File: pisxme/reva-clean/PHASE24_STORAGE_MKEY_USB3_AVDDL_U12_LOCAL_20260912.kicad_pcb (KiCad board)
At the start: 6 copper layers, 300 x 180 mm, 131 parts, among them J1 74221-101LF, J2 A70-112-331N126, J3 1-2199230-4, J4 Amphenol 10171746-00021LF USB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, J5 0039300020, J6 0039300020, J7 Raspberry-Pi-5-Compute-Module, Q1 CSD19536KCS, Q2 CSD19536KCS, U1 LM74700QDBVRQ1, U2 LM74700QDBVRQ1, U3 TPSM63606RDLR, U4 TPSM63606RDLR, U5 TPSM63606RDLR, U6 TPD4EUSB30, U7 TUSB9261IPVP, U8 Texas_DRT_3, U9 TPD4EUSB30, Y10 25MHz

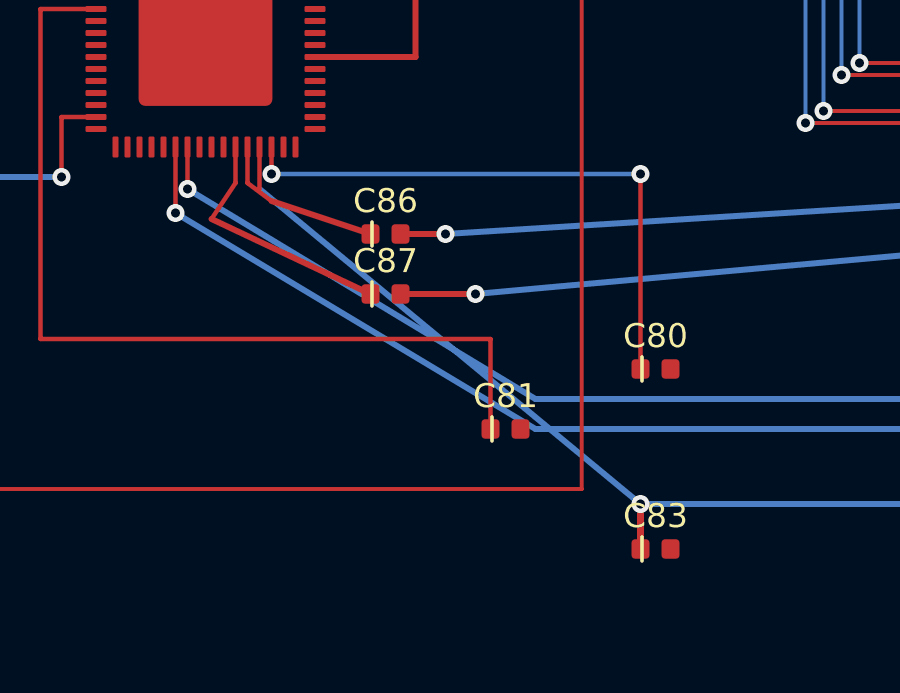
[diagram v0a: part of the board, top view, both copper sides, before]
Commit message: phase24: preserve cumulative AVDDL branches
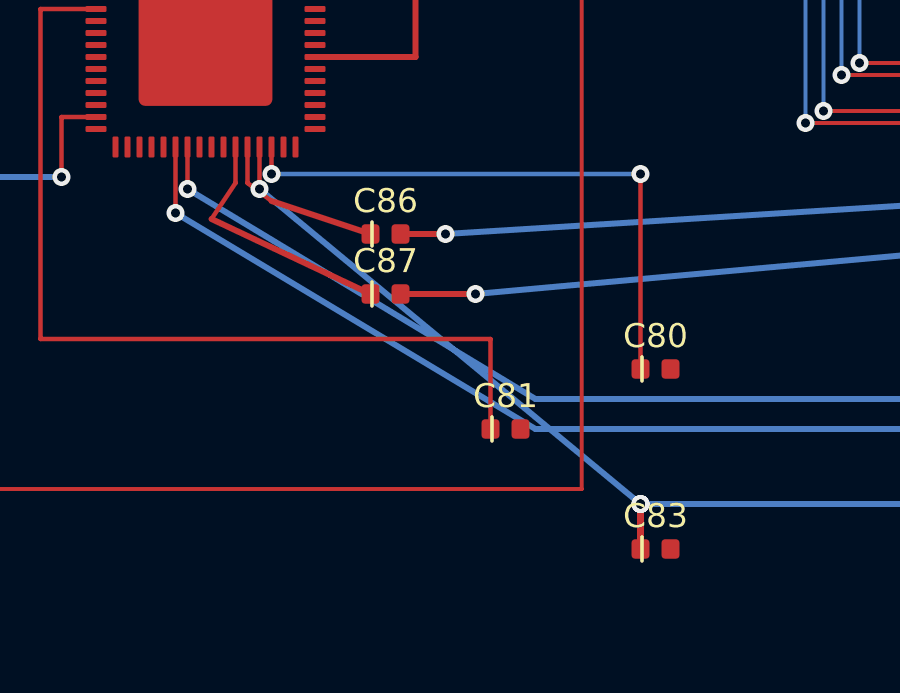
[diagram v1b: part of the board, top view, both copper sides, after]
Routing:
- net JMS_AVDDL: vias 2 -> 4
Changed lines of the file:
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@@
-	)
-	(segment
-		(start 166.5 132.6)
-		(end 168 132.6)
-		(width 0.15)
-		(layer "F.Cu")
-		(net "JMS_AVDDL")
 	)
 	(segment
@@
 		(width 0.2)
 		(layer "F.Cu")
+		(net "JMS_AVDDL")
+	)
+	(segment
+		(start 166.5 132.6)
+		(end 168 132.6)
+		(width 0.15)
+		(layer "F.Cu")
+		(net "JMS_AVDDL")
+	)
+	(via
+		(at 154.5 150.5)
+		(size 0.6)
+		(drill 0.3)
+		(layers "F.Cu" "B.Cu")
 		(net "JMS_AVDDL")
 	)
@@
 		(net "JMS_AVDDL")
 	)
+	(via
+		(at 141.8 140)
+		(size 0.6)
+		(drill 0.3)
+		(layers "F.Cu" "B.Cu")
+		(net "JMS_AVDDL")
+	)
 	(segment
-		(start 141.8 140)
-		(end 154.5 150.5)
+		(start 168 132.6)
+		(end 168 150.5)
 		(width 0.2)
 		(layer "B.Cu")
@@
 	)
 	(segment
-		(start 168 132.6)
-		(end 168 150.5)
+		(start 141.8 140)
+		(end 154.5 150.5)
 		(width 0.2)
 		(layer "B.Cu")
